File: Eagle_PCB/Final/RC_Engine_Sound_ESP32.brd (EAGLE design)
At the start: 80 x 59.7 mm, 84 parts, among them IC1 7805T, IC2 PAM8403, Q1 BC337-25, Q10 BC337-25, Q11 IRLZ44N, Q12 BC337-25, Q13 BC337-25, Q2 BC337-25, Q3 BC337-25, Q4 BC337-25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

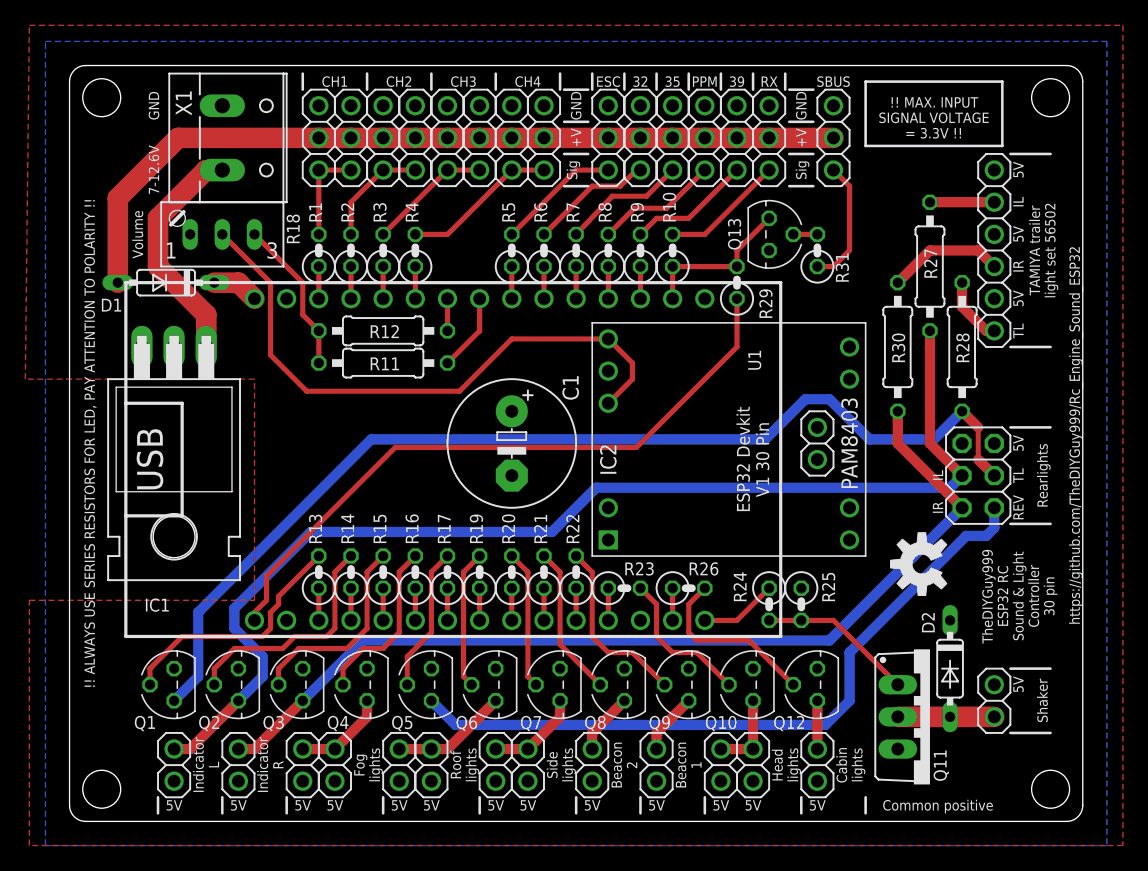
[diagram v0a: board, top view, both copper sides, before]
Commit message: PCB v1.1: moved R28 away from trailer connector
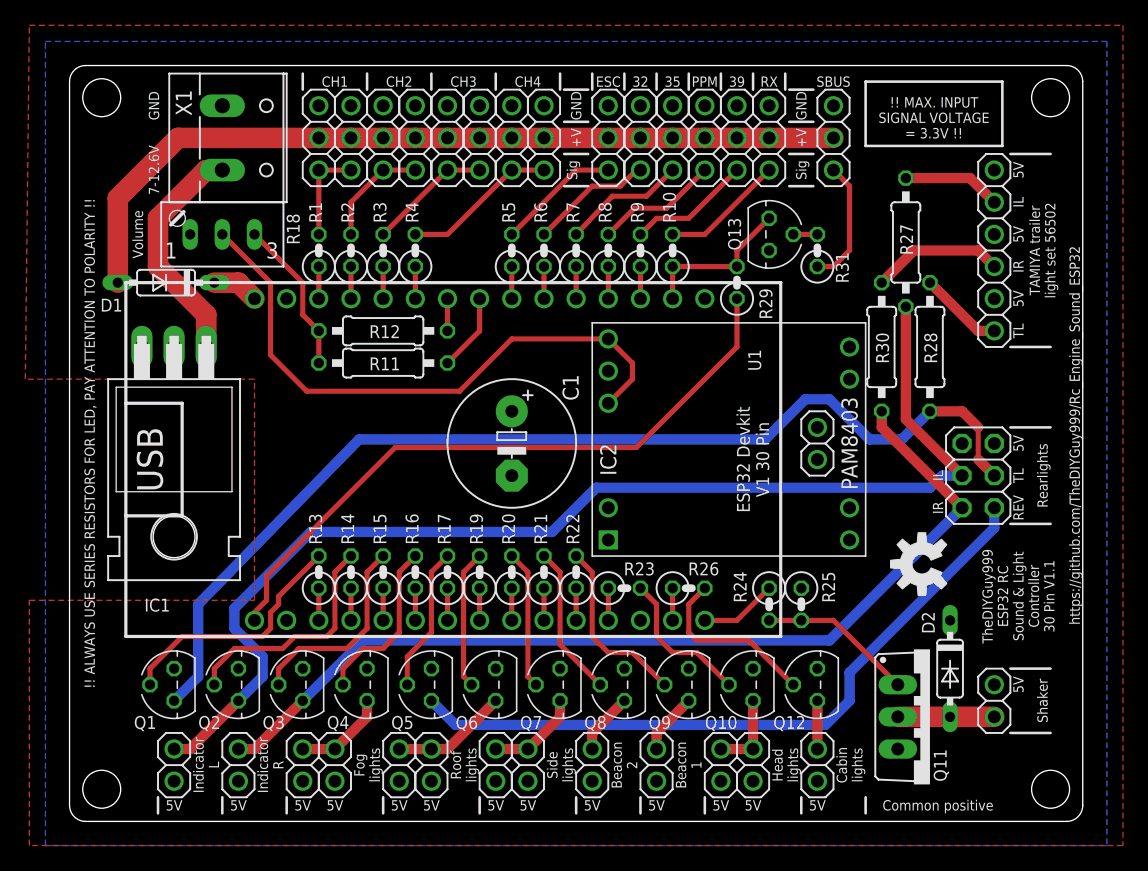
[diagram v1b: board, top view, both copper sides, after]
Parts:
- R29: value 10k -> 4k7
- moved R27 2.69 mm to (66.7, 45.1)
- moved R28 2.54 mm to (68.6, 36.8)
- moved R30 1.27 mm to (64.8, 36.8)
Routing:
- net INDICATOR_L: track 90.0 -> 92.7 mm
- net N$21: track 5.08 -> 7.77 mm
- net N$25: track 5.23 -> 6.66 mm
- net N$23: track 9.20 -> 10.5 mm
- net REVERSING: track 55.5 -> 54.6 mm
- net INDICATOR_R: track 74.8 -> 75.3 mm
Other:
- board text added: "TheDIYGuy999 ESP32 RC Sound & Light Controller 30 Pin V1.1"
- board text removed: "TheDIYGuy999 ESP32 RC Sound & Light Controller 30 pin"
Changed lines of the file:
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@@
 Sound &amp; Light
 Controller
-30 pin
+30 Pin V1.1
 </text>
 <text x="80.01" y="29.845" size="0.8128" layer="25" rot="R90" align="center">https://github.com/TheDIYGuy999/Rc_Engine_Sound_ESP32
@@
 <attribute name="VALUE" x="70.485" y="52.07" size="1.27" layer="27" rot="R270"/>
 </element>
-<element name="R27" library="rcl" package="0207/10" value="200R" x="68.58" y="43.18" smashed="yes" rot="R90">
-<attribute name="NAME" x="69.1515" y="42.1767" size="1.016" layer="25" ratio="10" rot="R90"/>
-</element>
-<element name="R30" library="rcl" package="0207/10" value="200R" x="66.04" y="36.83" smashed="yes" rot="R90">
-<attribute name="NAME" x="66.6115" y="35.5092" size="1.016" layer="25" ratio="10" rot="R90"/>
-</element>
-<element name="R28" library="rcl" package="0207/10" value="47R" x="71.12" y="36.83" smashed="yes" rot="R90">
-<attribute name="NAME" x="71.6915" y="35.5092" size="1.016" layer="25" ratio="10" rot="R90"/>
+<element name="R27" library="rcl" package="0207/10" value="200R" x="66.675" y="45.085" smashed="yes" rot="R90">
+<attribute name="NAME" x="67.2465" y="44.0817" size="1.016" layer="25" ratio="10" rot="R90"/>
+</element>
+<element name="R30" library="rcl" package="0207/10" value="200R" x="64.77" y="36.83" smashed="yes" rot="R90">
+<attribute name="NAME" x="65.3415" y="35.5092" size="1.016" layer="25" ratio="10" rot="R90"/>
+</element>
+<element name="R28" library="rcl" package="0207/10" value="47R" x="68.58" y="36.83" smashed="yes" rot="R90">
+<attribute name="NAME" x="69.1515" y="35.5092" size="1.016" layer="25" ratio="10" rot="R90"/>
 </element>
 <element name="JP20" library="00_custom_pinhead" package="2X03" value="" x="72.39" y="26.67" smashed="yes" rot="R90">
@@
 <attribute name="NAME" x="62.1665" y="41.8592" size="1.016" layer="25" ratio="10" rot="R90"/>
 </element>
-<element name="R29" library="rcl" package="0207/2V" value="10k" x="53.34" y="41.91" smashed="yes" rot="R90">
+<element name="R29" library="rcl" package="0207/2V" value="4k7" x="53.34" y="41.91" smashed="yes" rot="R90">
 <attribute name="NAME" x="56.134" y="39.0017" size="1.016" layer="25" ratio="10" rot="R90"/>
 </element>
@@
 <contactref element="R28" pad="1"/>
 <contactref element="JP20" pad="3"/>
+<wire x1="68.58" y1="31.75" x2="71.12" y2="31.75" width="0.8128" layer="1"/>
 <wire x1="71.12" y1="31.75" x2="72.39" y2="30.48" width="0.8128" layer="1"/>
 <wire x1="72.39" y1="30.48" x2="72.39" y2="27.94" width="0.4064" layer="1"/>
 <wire x1="72.39" y1="27.94" x2="73.66" y2="26.67" width="0.8128" layer="1"/>
 <wire x1="8.89" y1="8.89" x2="10.795" y2="10.795" width="0.8128" layer="16"/>
-<wire x1="10.795" y1="10.795" x2="10.795" y2="15.875" width="0.8128" layer="16"/>
-<wire x1="10.795" y1="15.875" x2="24.4475" y2="29.5275" width="0.8128" layer="16"/>
-<wire x1="24.4475" y1="29.5275" x2="55.5625" y2="29.5275" width="0.8128" layer="16"/>
+<wire x1="10.795" y1="10.795" x2="10.795" y2="16.51" width="0.8128" layer="16"/>
+<wire x1="10.795" y1="16.51" x2="23.495" y2="29.5275" width="0.8128" layer="16"/>
+<wire x1="23.495" y1="29.5275" x2="55.5625" y2="29.5275" width="0.8128" layer="16"/>
 <wire x1="55.5625" y1="29.5275" x2="58.7375" y2="32.7025" width="0.8128" layer="16"/>
 <wire x1="58.7375" y1="32.7025" x2="60.6425" y2="32.7025" width="0.8128" layer="16"/>
 <wire x1="60.6425" y1="32.7025" x2="63.8175" y2="29.5275" width="0.8128" layer="16"/>
-<wire x1="63.8175" y1="29.5275" x2="68.8975" y2="29.5275" width="0.8128" layer="16"/>
-<wire x1="68.8975" y1="29.5275" x2="71.12" y2="31.75" width="0.8128" layer="16"/>
+<wire x1="63.8175" y1="29.5275" x2="66.3575" y2="29.5275" width="0.8128" layer="16"/>
+<wire x1="66.3575" y1="29.5275" x2="68.58" y2="31.75" width="0.8128" layer="16"/>
 </signal>
 <signal name="N$22">
@@
 <contactref element="R27" pad="1"/>
 <contactref element="JP20" pad="4"/>
-<wire x1="68.58" y1="38.1" x2="68.58" y2="29.21" width="0.8128" layer="1"/>
-<wire x1="68.58" y1="29.21" x2="71.12" y2="26.67" width="0.8128" layer="1"/>
+<wire x1="66.675" y1="40.005" x2="66.675" y2="31.115" width="0.8128" layer="1"/>
+<wire x1="66.675" y1="31.115" x2="71.12" y2="26.67" width="0.8128" layer="1"/>
 <wire x1="13.97" y1="8.89" x2="15.875" y2="10.795" width="0.8128" layer="16"/>
 <wire x1="15.875" y1="10.795" x2="15.875" y2="12.3825" width="0.8128" layer="16"/>
@@
 <wire x1="19.685" y1="22.225" x2="38.735" y2="22.225" width="0.8128" layer="16"/>
 <wire x1="38.735" y1="22.225" x2="42.2275" y2="25.7175" width="0.8128" layer="16"/>
-<wire x1="42.2275" y1="25.7175" x2="70.1675" y2="25.7175" width="0.8128" layer="16"/>
-<wire x1="70.1675" y1="25.7175" x2="71.12" y2="26.67" width="0.8128" layer="16"/>
+<wire x1="42.2275" y1="25.7175" x2="68.58" y2="25.7175" width="0.8128" layer="16"/>
+<wire x1="68.58" y1="25.7175" x2="69.5325" y2="26.67" width="0.8128" layer="16"/>
+<wire x1="69.5325" y1="26.67" x2="71.12" y2="26.67" width="0.8128" layer="16"/>
 <wire x1="13.97" y1="8.89" x2="10.16" y2="5.08" width="0.8128" layer="1"/>
 <wire x1="10.16" y1="5.08" x2="8.89" y2="5.08" width="0.8128" layer="1"/>
@@
 <contactref element="R30" pad="1"/>
 <contactref element="JP20" pad="2"/>
-<wire x1="66.04" y1="31.75" x2="66.04" y2="29.21" width="0.8128" layer="1"/>
-<wire x1="66.04" y1="29.21" x2="71.12" y2="24.13" width="0.8128" layer="1"/>
+<wire x1="64.77" y1="31.75" x2="64.77" y2="30.48" width="0.8128" layer="1"/>
+<wire x1="64.77" y1="30.48" x2="71.12" y2="24.13" width="0.8128" layer="1"/>
 <wire x1="19.05" y1="8.89" x2="23.8125" y2="13.6525" width="0.8128" layer="16"/>
 <wire x1="23.8125" y1="13.6525" x2="60.6425" y2="13.6525" width="0.8128" layer="16"/>
@@
 <wire x1="31.115" y1="6.985" x2="60.325" y2="6.985" width="0.8128" layer="16"/>
 <wire x1="60.325" y1="6.985" x2="62.23" y2="8.89" width="0.8128" layer="16"/>
-<wire x1="62.23" y1="8.89" x2="62.23" y2="12.7" width="0.8128" layer="16"/>
-<wire x1="62.23" y1="12.7" x2="71.4375" y2="21.9075" width="0.8128" layer="16"/>
-<wire x1="71.4375" y1="21.9075" x2="73.025" y2="21.9075" width="0.8128" layer="16"/>
+<wire x1="62.23" y1="8.89" x2="62.23" y2="11.1125" width="0.8128" layer="16"/>
+<wire x1="62.23" y1="11.1125" x2="73.66" y2="22.5425" width="0.8128" layer="16"/>
 <wire x1="73.66" y1="24.13" x2="73.66" y2="22.5425" width="0.8128" layer="16"/>
-<wire x1="73.66" y1="22.5425" x2="73.025" y2="21.9075" width="0.8128" layer="16"/>
 </signal>
 <signal name="N$23">
 <contactref element="JP30" pad="4"/>
 <contactref element="R30" pad="2"/>
-<wire x1="68.58" y1="44.45" x2="66.04" y2="41.91" width="0.8128" layer="1"/>
-<wire x1="68.58" y1="44.45" x2="72.39" y2="44.45" width="0.8128" layer="1"/>
+<wire x1="67.31" y1="44.45" x2="64.77" y2="41.91" width="0.8128" layer="1"/>
+<wire x1="67.31" y1="44.45" x2="72.39" y2="44.45" width="0.8128" layer="1"/>
 <wire x1="72.39" y1="44.45" x2="73.66" y2="43.18" width="0.8128" layer="1"/>
 </signal>
@@
 <contactref element="JP30" pad="6"/>
 <contactref element="R28" pad="2"/>
-<wire x1="73.66" y1="38.1" x2="73.025" y2="38.1" width="0.8128" layer="1"/>
-<wire x1="73.025" y1="38.1" x2="71.12" y2="40.005" width="0.8128" layer="1"/>
-<wire x1="71.12" y1="40.005" x2="71.12" y2="41.91" width="0.8128" layer="1"/>
+<wire x1="73.66" y1="38.1" x2="72.39" y2="38.1" width="0.8128" layer="1"/>
+<wire x1="72.39" y1="38.1" x2="68.58" y2="41.91" width="0.8128" layer="1"/>
 </signal>
 <signal name="N$21">
 <contactref element="JP30" pad="2"/>
 <contactref element="R27" pad="2"/>
-<wire x1="68.58" y1="48.26" x2="73.66" y2="48.26" width="0.8128" layer="1"/>
+<wire x1="66.675" y1="50.165" x2="71.755" y2="50.165" width="0.8128" layer="1"/>
+<wire x1="71.755" y1="50.165" x2="73.66" y2="48.26" width="0.8128" layer="1"/>
 </signal>
 <signal name="D1">
